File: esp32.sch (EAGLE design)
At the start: 4 parts, among them U1 ESP32MOD

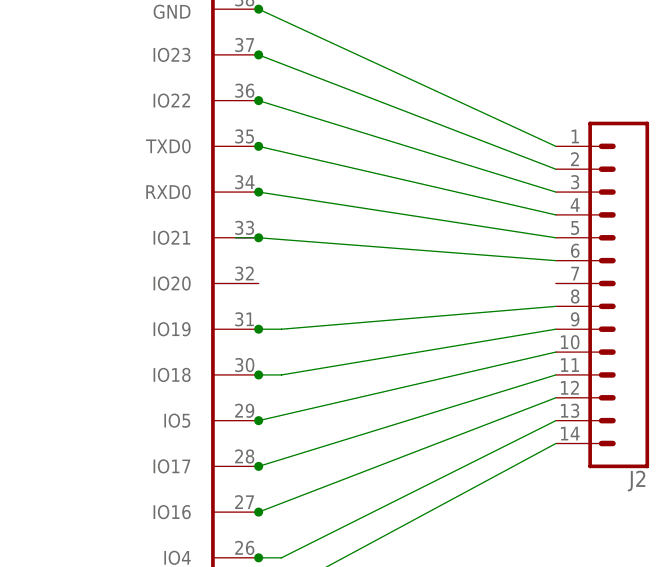
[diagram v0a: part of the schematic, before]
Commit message: ground clearance between pads increased and GPIO 20 connected
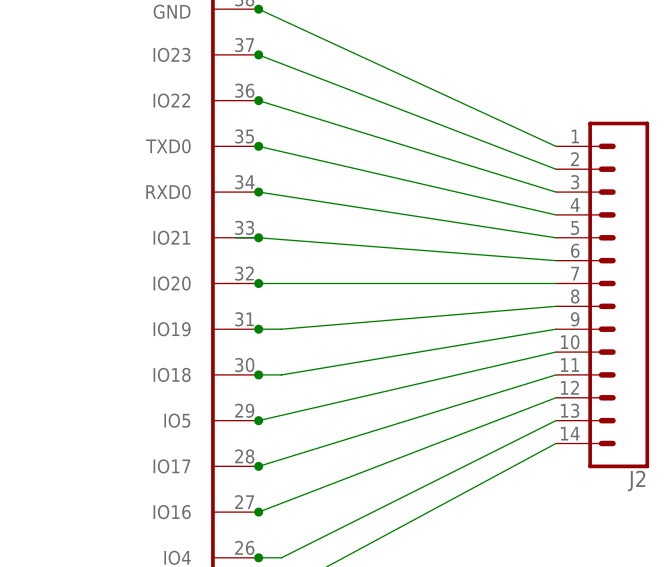
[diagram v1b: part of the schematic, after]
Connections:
- new net N$1: J2.7, U1.IO20
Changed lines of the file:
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@@
 <grid distance="0.1" unitdist="inch" unit="inch" style="lines" multiple="1" display="no" altdistance="0.01" altunitdist="inch" altunit="inch"/>
 <layers>
-<layer number="1" name="Top" color="4" fill="1" visible="yes" active="no"/>
-<layer number="16" name="Bottom" color="1" fill="1" visible="yes" active="no"/>
-<layer number="17" name="Pads" color="2" fill="1" visible="yes" active="no"/>
-<layer number="18" name="Vias" color="2" fill="1" visible="yes" active="no"/>
-<layer number="19" name="Unrouted" color="6" fill="1" visible="yes" active="no"/>
-<layer number="20" name="Dimension" color="15" fill="1" visible="yes" active="no"/>
-<layer number="21" name="tPlace" color="7" fill="1" visible="yes" active="no"/>
-<layer number="22" name="bPlace" color="7" fill="1" visible="yes" active="no"/>
-<layer number="23" name="tOrigins" color="15" fill="1" visible="yes" active="no"/>
-<layer number="24" name="bOrigins" color="15" fill="1" visible="yes" active="no"/>
-<layer number="25" name="tNames" color="7" fill="1" visible="yes" active="no"/>
-<layer number="26" name="bNames" color="7" fill="1" visible="yes" active="no"/>
-<layer number="27" name="tValues" color="7" fill="1" visible="yes" active="no"/>
-<layer number="28" name="bValues" color="7" fill="1" visible="yes" active="no"/>
+<layer number="1" name="Top" color="4" fill="1" visible="no" active="no"/>
+<layer number="16" name="Bottom" color="1" fill="1" visible="no" active="no"/>
+<layer number="17" name="Pads" color="2" fill="1" visible="no" active="no"/>
+<layer number="18" name="Vias" color="2" fill="1" visible="no" active="no"/>
+<layer number="19" name="Unrouted" color="6" fill="1" visible="no" active="no"/>
+<layer number="20" name="Dimension" color="15" fill="1" visible="no" active="no"/>
+<layer number="21" name="tPlace" color="7" fill="1" visible="no" active="no"/>
+<layer number="22" name="bPlace" color="7" fill="1" visible="no" active="no"/>
+<layer number="23" name="tOrigins" color="15" fill="1" visible="no" active="no"/>
+<layer number="24" name="bOrigins" color="15" fill="1" visible="no" active="no"/>
+<layer number="25" name="tNames" color="7" fill="1" visible="no" active="no"/>
+<layer number="26" name="bNames" color="7" fill="1" visible="no" active="no"/>
+<layer number="27" name="tValues" color="7" fill="1" visible="no" active="no"/>
+<layer number="28" name="bValues" color="7" fill="1" visible="no" active="no"/>
 <layer number="29" name="tStop" color="7" fill="3" visible="no" active="no"/>
 <layer number="30" name="bStop" color="7" fill="6" visible="no" active="no"/>
@@
 <layer number="35" name="tGlue" color="7" fill="4" visible="no" active="no"/>
 <layer number="36" name="bGlue" color="7" fill="5" visible="no" active="no"/>
-<layer number="37" name="tTest" color="7" fill="1" visible="yes" active="no"/>
-<layer number="38" name="bTest" color="7" fill="1" visible="yes" active="no"/>
+<layer number="37" name="tTest" color="7" fill="1" visible="no" active="no"/>
+<layer number="38" name="bTest" color="7" fill="1" visible="no" active="no"/>
 <layer number="39" name="tKeepout" color="4" fill="11" visible="no" active="no"/>
 <layer number="40" name="bKeepout" color="1" fill="11" visible="no" active="no"/>
@@
 <layer number="44" name="Drills" color="7" fill="1" visible="no" active="no"/>
 <layer number="45" name="Holes" color="7" fill="1" visible="no" active="no"/>
-<layer number="46" name="Milling" color="3" fill="1" visible="yes" active="no"/>
-<layer number="47" name="Measures" color="7" fill="1" visible="yes" active="no"/>
-<layer number="48" name="Document" color="7" fill="1" visible="yes" active="no"/>
-<layer number="49" name="Reference" color="7" fill="1" visible="yes" active="no"/>
-<layer number="50" name="dxf" color="7" fill="1" visible="yes" active="no"/>
-<layer number="51" name="tDocu" color="7" fill="1" visible="yes" active="no"/>
-<layer number="52" name="bDocu" color="7" fill="1" visible="yes" active="no"/>
-<layer number="53" name="tGND_GNDA" color="7" fill="9" visible="yes" active="no"/>
-<layer number="54" name="bGND_GNDA" color="1" fill="9" visible="yes" active="no"/>
-<layer number="56" name="wert" color="7" fill="1" visible="yes" active="no"/>
-<layer number="57" name="tCAD" color="7" fill="1" visible="yes" active="no"/>
-<layer number="59" name="tCarbon" color="7" fill="1" visible="yes" active="no"/>
-<layer number="60" name="bCarbon" color="7" fill="1" visible="yes" active="no"/>
+<layer number="46" name="Milling" color="3" fill="1" visible="no" active="no"/>
+<layer number="47" name="Measures" color="7" fill="1" visible="no" active="no"/>
+<layer number="48" name="Document" color="7" fill="1" visible="no" active="no"/>
+<layer number="49" name="Reference" color="7" fill="1" visible="no" active="no"/>
+<layer number="50" name="dxf" color="7" fill="1" visible="no" active="no"/>
+<layer number="51" name="tDocu" color="7" fill="1" visible="no" active="no"/>
+<layer number="52" name="bDocu" color="7" fill="1" visible="no" active="no"/>
+<layer number="53" name="tGND_GNDA" color="7" fill="9" visible="no" active="no"/>
+<layer number="54" name="bGND_GNDA" color="1" fill="9" visible="no" active="no"/>
+<layer number="56" name="wert" color="7" fill="1" visible="no" active="no"/>
+<layer number="57" name="tCAD" color="7" fill="1" visible="no" active="no"/>
+<layer number="59" name="tCarbon" color="7" fill="1" visible="no" active="no"/>
+<layer number="60" name="bCarbon" color="7" fill="1" visible="no" active="no"/>
 <layer number="90" name="Modules" color="5" fill="1" visible="yes" active="yes"/>
 <layer number="91" name="Nets" color="2" fill="1" visible="yes" active="yes"/>
@@
 </segment>
 </net>
+<net name="N$1" class="0">
+<segment>
+<pinref part="J2" gate="G$1" pin="7"/>
+<pinref part="U1" gate="G$1" pin="IO20"/>
+<wire x1="134.62" y1="40.64" x2="101.6" y2="40.64" width="0.1524" layer="91"/>
+<junction x="101.6" y="40.64"/>
+</segment>
+</net>
